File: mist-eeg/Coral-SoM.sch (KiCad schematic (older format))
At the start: 5 parts, among them J6 Conn_02x40_Counter_Clockwise, J7 J1312, J8 J1311, J9 J1310, SW3 RESET

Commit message: Hooked-up the SoM
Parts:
- removed J6: Conn_02x40_Counter_Clockwise, symbol Connector_Generic:Conn_02x40_Counter_Clockwise
- added J6: Extra GPIOs, symbol Connector:Conn_01x03_Female
- added J7: Digital buses, symbol Connector_Generic:Conn_02x03_Top_Bottom
- added R104, R107: 0R, symbol Device:R_Small
- added R105, R106, R108, R109, R111: DNF, symbol Device:R_Small
- added R110, R112: 4k7, symbol Device:R_Small
- added SW?: SW_Push, symbol Switch:SW_Push
- added TP12: ~POR~, symbol Connector:TestPoint
- renumbered J9 to J10, J7 to J8, J8 to J9, SW3 to SW4
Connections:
- net labels added: +3V3_IN, AUDIO_MCLK, BOOT_MODE0, BOOT_MODE1, EXTRA_1, EXTRA_2, EXTRA_3, JTAG_TCK, JTAG_TDI, JTAG_TDO, JTAG_TMS, ONOFF, RXD, SD_CLK, SD_CMD, SD_DAT0, SD_DAT1, SD_DAT2, SD_DAT3, TXD, USB1_DN, USB1_DP, USB1_ID, USB1_RXN, USB1_RXP, USB1_TXN, USB1_TXP, USB1_VBUS, ~JTAG_TRST~, ~POR~, ~PWR_ON~, ~SD_CONNECTED~, ~SD_RST~
- net labels removed: SD_DATA_CLK, SD_DATA_CMD, SD_DATA_CONNECTED, SD_DATA_DAT0, SD_DATA_DAT1, SD_DATA_DAT2, SD_DATA_DAT3
- wire segments 243 -> 320
- no-connect marks 52 -> 151
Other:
- note added: "SPI1 => EEG\nUSB1 => Power?\nSAI2 => Audio\nSD2 => SD card\nJTAG => Header?\nI2C2 => Audio I2C\nI2C3 => Control I2C\nUART1 => Serial console\nPWM1 => USER1_R\nPWM2 => USER1_G\nPWM3 => USER1_B\nPWM4 => Extra 1\nGPIO6 => USER2_R\nGPIO7 => USER2_G\nGPIO8 => USER2_B\nGPIO12 => USER\nNAND_CLE => USER3_R\nNAND_DATA02 => USER3_G\nNAND_ALE => USER3_B\nNAND_DATA07 => START\nNAND_DATA06 => ~EEG_PWDN~\nNAND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"
- moved on the sheet: J8, J9

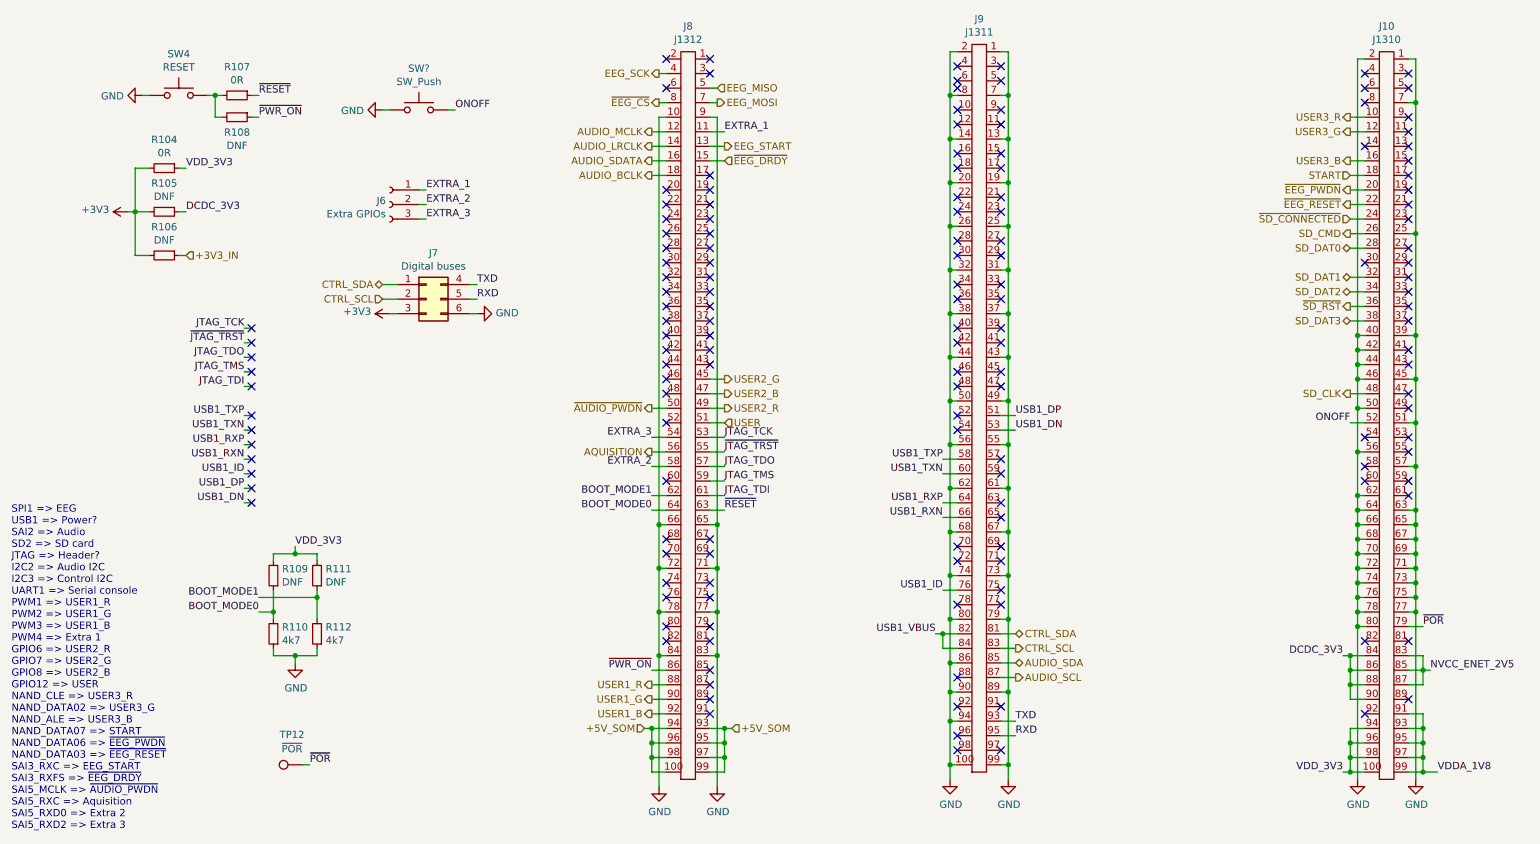
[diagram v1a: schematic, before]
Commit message: Finish schematic and create interface specifications
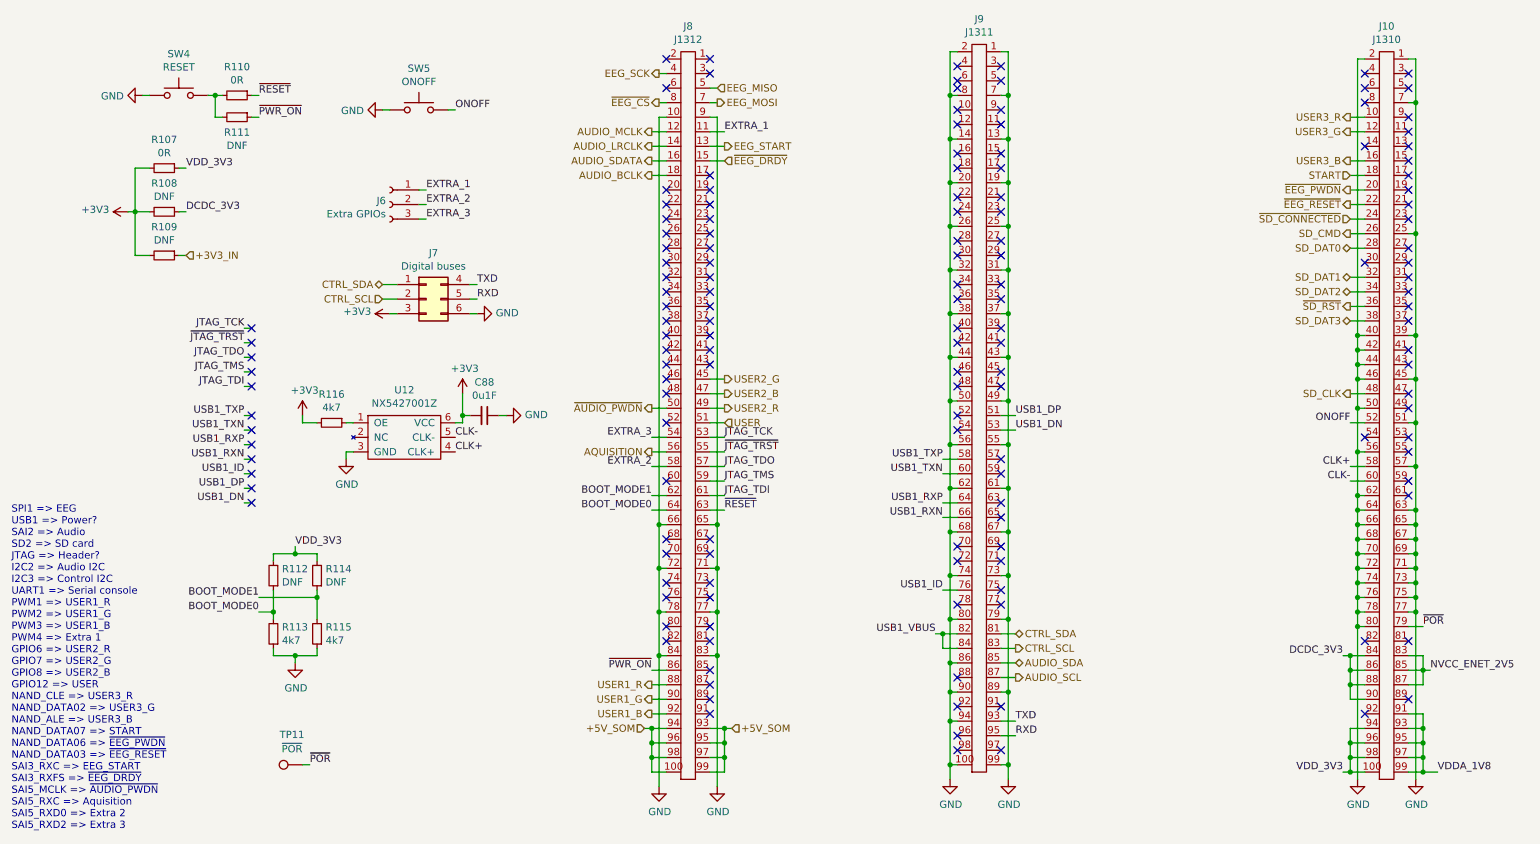
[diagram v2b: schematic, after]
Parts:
- added C88: 0u1F, Capacitor_SMD:C_0201_0603Metric, symbol Device:C_Small
- added R116: 4k7, Resistor_SMD:R_0201_0603Metric, symbol Device:R_Small
- added U12: NX5427001Z, mist-eeg:NX5427001Z, symbol components:NX5427001Z
- J10, J8, J9: footprint (none) -> mist-eeg:DF40HC3.0-100DS-0.4V58
- J6: footprint (none) -> Connector_PinHeader_2.54mm:PinHeader_1x03_P2.54mm_Vertical
- J7: footprint (none) -> Connector_PinHeader_2.54mm:PinHeader_2x03_P2.54mm_Vertical
- R107: renamed from R104; footprint (none) -> Resistor_SMD:R_0603_1608Metric
- R108: renamed from R105; footprint (none) -> Resistor_SMD:R_0603_1608Metric
- R109: renamed from R106; footprint (none) -> Resistor_SMD:R_0603_1608Metric
- R110: renamed from R107; footprint (none) -> Resistor_SMD:R_0603_1608Metric
- R111: renamed from R108; footprint (none) -> Resistor_SMD:R_0603_1608Metric
- R112: renamed from R109; footprint (none) -> Resistor_SMD:R_0603_1608Metric
- R113: renamed from R110; footprint (none) -> Resistor_SMD:R_0201_0603Metric
- R114: renamed from R111; footprint (none) -> Resistor_SMD:R_0603_1608Metric
- R115: renamed from R112; footprint (none) -> Resistor_SMD:R_0201_0603Metric
- SW5: renamed from SW?; value SW_Push -> ONOFF; footprint (none) -> Connector_PinHeader_1.27mm:PinHeader_1x02_P1.27mm_Vertical
- TP11: renamed from TP12; footprint (none) -> TestPoint:TestPoint_Pad_D1.0mm
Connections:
- net +3V3: now also C88.2, R116.2, U12.6 (VCC)
- net GND: now also C88.1, U12.3 (GND)
- net CLK+: now reaches J10.58
- net CLK+: now also U12.4 (CLK+)
- net CLK-: now reaches J10.60
- net CLK-: now also U12.5 (CLK-)
- new net: R116.1, U12.1 (OE)
- no-connect marks 151 -> 149

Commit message: Advance routing
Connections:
- net +3V3: now also R112.2, R114.2
- net CTRL_SCL: now also J7.6 (Pin_6); no longer J7.2 (Pin_2)
- net CTRL_SDA: now also J7.5 (Pin_5); no longer J7.1 (Pin_1)
- net GND: now also J7.4 (Pin_4); no longer J7.6 (Pin_6)
- net RXD: now also J7.2 (Pin_2); no longer J7.5 (Pin_5)
- net TXD: now also J7.1 (Pin_1); no longer J7.4 (Pin_4)
- net USER3_B: now also J10.10; no longer J10.16
- net USER3_R: now also J10.16; no longer J10.10
- net VDD_3V3: no longer R112.2, R114.2
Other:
- note added: "SPI1 => EEG\nUSB1 => Power?\nSAI2 => Audio\nSD2 => SD card\nJTAG => Header?\nI2C2 => Audio I2C\nI2C3 => Control I2C\nUART1 => Serial console\nPWM1 => USER1_R\nPWM2 => USER1_G\nPWM3 => USER1_B\nPWM4 => Extra 1\nGPIO6 => USER2_R\nGPIO7 => USER2_G\nGPIO8 => USER2_B\nGPIO12 => USER\nNAND_ALE => USER3_R\nNAND_DATA02 => USER3_G\nNAND_CLE => USER3_B\nNAND_DATA07 => START\nNAND_DATA06 => ~EEG_PWDN~\nNAND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"
- note removed: "SPI1 => EEG\nUSB1 => Power?\nSAI2 => Audio\nSD2 => SD card\nJTAG => Header?\nI2C2 => Audio I2C\nI2C3 => Control I2C\nUART1 => Serial console\nPWM1 => USER1_R\nPWM2 => USER1_G\nPWM3 => USER1_B\nPWM4 => Extra 1\nGPIO6 => USER2_R\nGPIO7 => USER2_G\nGPIO8 => USER2_B\nGPIO12 => USER\nNAND_CLE => USER3_R\nNAND_DATA02 => USER3_G\nNAND_ALE => USER3_B\nNAND_DATA07 => START\nNAND_DATA06 => ~EEG_PWDN~\nNAND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"
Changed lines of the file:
@@
 $Descr A4 11693 8268
 encoding utf-8
-Sheet 12 12
+Sheet 11 11
 Title ""
 Date ""
@@
 Text HLabel 5500 3300 2    50   Output ~ 0
 USER2_B
-Text HLabel 9800 1400 0    50   Output ~ 0
+Text HLabel 9800 1700 0    50   Output ~ 0
 USER3_R
 Text HLabel 9800 1500 0    50   Output ~ 0
 USER3_G
-Text HLabel 9800 1700 0    50   Output ~ 0
+Text HLabel 9800 1400 0    50   Output ~ 0
 USER3_B
 Text HLabel 5000 3700 0    50   Output ~ 0
@@
 	10300 4900 10200 4900
 Text Notes 600  6300 0    50   ~ 0
-SPI1 => EEG\nUSB1 => Power?\nSAI2 => Audio\nSD2 => SD card\nJTAG => Header?\nI2C2 => Audio I2C\nI2C3 => Control I2C\nUART1 => Serial console\nPWM1 => USER1_R\nPWM2 => USER1_G\nPWM3 => USER1_B\nPWM4 => Extra 1\nGPIO6 => USER2_R\nGPIO7 => USER2_G\nGPIO8 => USER2_B\nGPIO12 => USER\nNAND_CLE => USER3_R\nNAND_DATA02 => USER3_G\nNAND_ALE => USER3_B\nNAND_DATA07 => START\nNAND_DATA06 => ~EEG_PWDN~\nNAND_DATA03 => ~EEG_RESET~\nSAI3_RXC => EEG_START\nSAI3_RXFS => ~EEG_DRDY~\nSAI5_MCLK => ~AUDIO_PWDN~\nSAI5_RXC => Aquisition\nSAI5_RXD0 => Extra 2\nSAI5_RXD2 => Extra 3
+SPI1 => EEG\nUSB1 => Power?\nSAI2 => Audio\nSD2 => SD card\nJTAG => Header?\nI2C2 => Audio I2C\nI2C3 => Control I2C\nUART1 => Serial console\nPWM1 => USER1_R\nPWM2 => USER1_G\nPWM3 => USER1_B\nPWM4 => Extra 1\nGPIO6 => USER2_R\nGPIO7 => USER2_G\nGPIO8 => USER2_B\nGPIO12 => USER\nNAND_ALE => USER3_R\nNAND_DATA02 => USER3_G\nNAND_CLE => USER3_B\nNAND_DATA07 => START\nNAND_DATA06 => ~EEG_PWDN~\nNAND_DATA03 => ~EEG_RESET~\nSAI3_RXC => EEG_START\nSAI3_RXFS => ~EEG_DRDY~\nSAI5_MCLK => ~AUDIO_PWDN~\nSAI5_RXC => Aquisition\nSAI5_RXD0 => Extra 2\nSAI5_RXD2 => Extra 3
 Text HLabel 5000 1500 0    50   Output ~ 0
 AUDIO_MCLK
@@
 	1    0    0    -1
 $EndComp
-Text Label 3800 2550 0    50   ~ 0
+Text Label 3200 2550 2    50   ~ 0
 TXD
-Text Label 3800 2650 0    50   ~ 0
+Text Label 3200 2650 2    50   ~ 0
 RXD
 Wire Wire Line
-	3800 2650 3750 2650
+	3200 2650 3250 2650
 Wire Wire Line
-	3750 2550 3800 2550
+	3250 2550 3200 2550
 Wire Wire Line
 	3200 2750 3250 2750
@@
 L power:GND #PWR0129
 U 1 1 627DBA20
-P 3800 2750
-F 0 "#PWR0129" H 3800 2500 50  0001 C CNN
-F 1 "GND" V 3805 2622 50  0000 R CNN
-F 2 "" H 3800 2750 50  0001 C CNN
-F 3 "" H 3800 2750 50  0001 C CNN
-	1    3800 2750
+P 3800 2550
+F 0 "#PWR0129" H 3800 2300 50  0001 C CNN
+F 1 "GND" V 3805 2422 50  0000 R CNN
+F 2 "" H 3800 2550 50  0001 C CNN
+F 3 "" H 3800 2550 50  0001 C CNN
+	1    3800 2550
 	0    -1   -1   0
 $EndComp
 Wire Wire Line
-	3800 2750 3750 2750
+	3800 2550 3750 2550
 Text HLabel 7500 5050 2    50   Output ~ 0
 CTRL_SCL
 Text HLabel 7500 4950 2    50   BiDi ~ 0
 CTRL_SDA
-Text HLabel 3150 2650 0    50   Input ~ 0
+Text HLabel 3850 2750 2    50   Input ~ 0
 CTRL_SCL
-Text HLabel 3150 2550 0    50   BiDi ~ 0
+Text HLabel 3850 2650 2    50   BiDi ~ 0
 CTRL_SDA
 Wire Wire Line
-	3150 2650 3250 2650
+	3850 2750 3750 2750
 Wire Wire Line
-	3150 2550 3250 2550
+	3850 2650 3750 2650
 NoConn ~ 10200 3900
 NoConn ~ 10200 4000
@@
 	2700 4700 2700 4650
 Connection ~ 2700 4700
-Text Label 2550 4350 0    50   ~ 0
-VDD_3V3
 Wire Wire Line
 	2550 4350 2550 4400
@@
 Wire Wire Line
 	2600 3500 2700 3500
+$Comp
+L power:+3V3 #PWR0137
+U 1 1 6104B8C8
+P 2550 4350
+F 0 "#PWR0137" H 2550 4200 50  0001 C CNN
+F 1 "+3V3" V 2565 4478 50  0000 L CNN
+F 2 "" H 2550 4350 50  0001 C CNN
+F 3 "" H 2550 4350 50  0001 C CNN
+	1    2550 4350
+	1    0    0    -1
+$EndComp
 $EndSCHEMATC

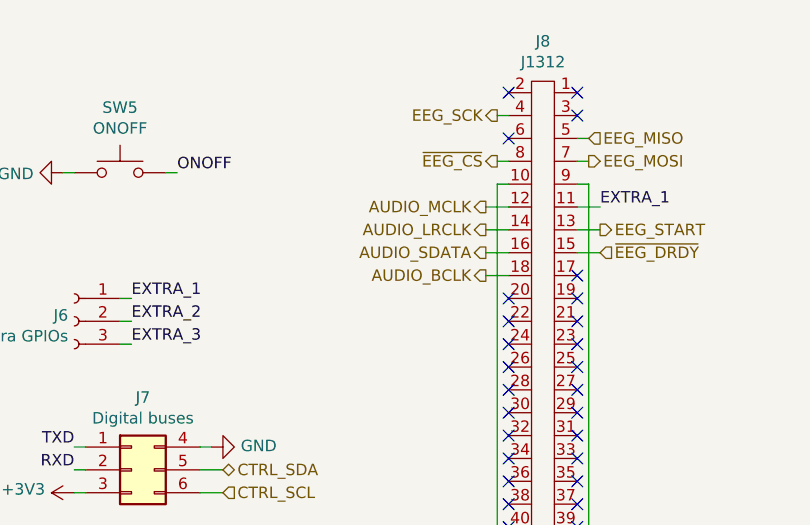
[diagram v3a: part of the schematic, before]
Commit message: Small fix to the TPS63070 footprint
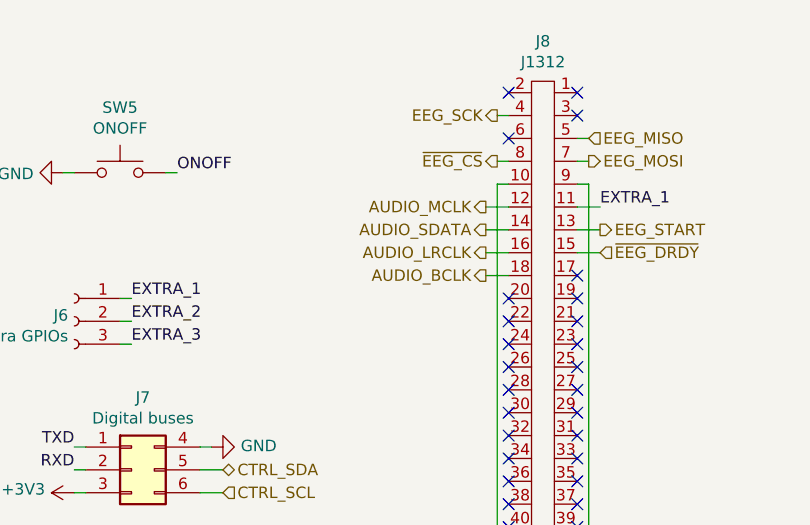
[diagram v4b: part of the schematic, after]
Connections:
- net AUDIO_LRCLK: now also J8.16; no longer J8.14
- net AUDIO_SDATA: now also J8.14; no longer J8.16
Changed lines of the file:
@@
 Text HLabel 5000 1800 0    50   Output ~ 0
 AUDIO_BCLK
+Text HLabel 5000 1700 0    50   Output ~ 0
+AUDIO_LRCLK
 Text HLabel 5000 1600 0    50   Output ~ 0
-AUDIO_LRCLK
-Text HLabel 5000 1700 0    50   Output ~ 0
 AUDIO_SDATA
 Text HLabel 5000 3400 0    50   Output ~ 0

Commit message: Change buckboost regulator used
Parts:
- J5: renamed from J6; footprint Connector_PinHeader_2.54mm:PinHeader_1x03_P2.54mm_Vertical -> Connector_PinHeader_2.54mm:PinHeader_2x02_P2.54mm_Vertical; symbol Connector:Conn_01x03_Female -> Connector:Conn_01x04_Female
- renumbered C88 to C81, J7 to J6, J8 to J7, J9 to J8, J10 to J9, R107 to R83, R108 to R84, R109 to R85, R110 to R86, R111 to R87, R112 to R88, R113 to R89, R114 to R90, R115 to R91, R116 to R92, TP11 to TP7, U12 to U9
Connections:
- net EXTRA_1: now also J7.58; no longer J7.11
- net EXTRA_2: now also J7.11; no longer J7.58
- net ~AUDIO_PWDN~ renamed EXTRA_4
- net EXTRA_4: now also J5.4 (Pin_4)
